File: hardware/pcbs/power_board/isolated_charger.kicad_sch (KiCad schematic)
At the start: 12 parts, among them J4 USB_A, U1 VRB1205S-6WR3, U2 LTV-247, U3 NCP380

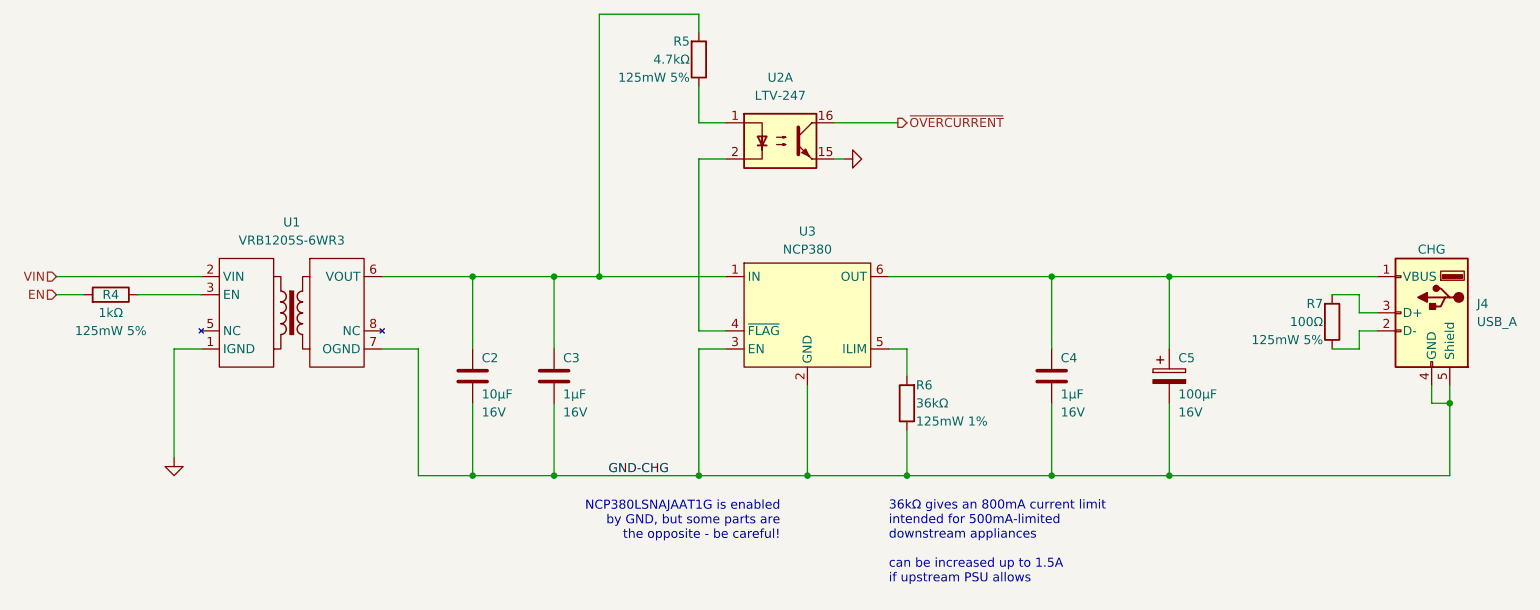
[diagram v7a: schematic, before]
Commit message: power_board: add protection resistor to overload signal
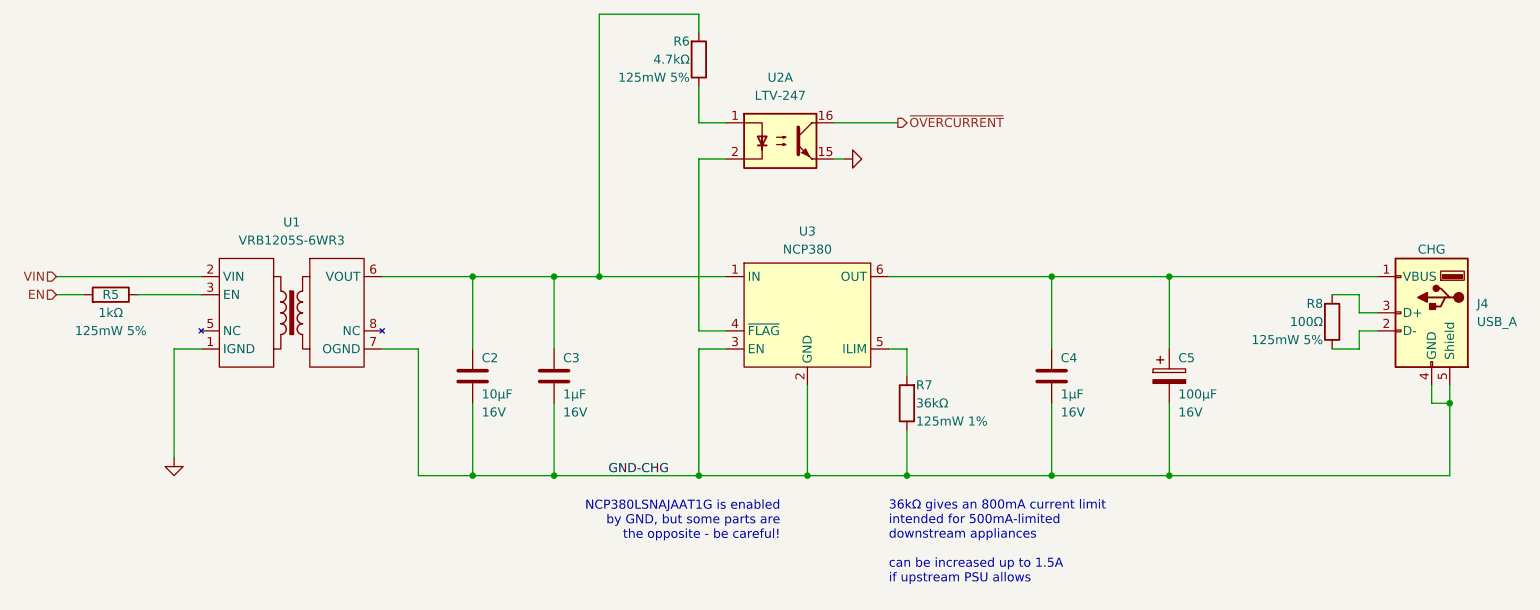
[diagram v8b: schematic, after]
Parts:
- renumbered R4 to R5, R5 to R6, R6 to R7, R7 to R8
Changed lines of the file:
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@@
 		(on_board yes)
 		(dnp no)
-		(property "Reference" "R4"
+		(property "Reference" "R5"
 			(at 69.85 91.44 90)
 			(effects
@@
 			(project "power_board"
 				(path "/4b166175-80a4-48c6-994d-6e62a6160b87/2e2b9578-5dbd-4b2d-88fb-256ac9c8dd75/32f9baea-32bc-4a84-b83a-18c67cc6248e"
-					(reference "R4")
+					(reference "R5")
 					(unit 1)
 				)
 				(path "/4b166175-80a4-48c6-994d-6e62a6160b87/2e2b9578-5dbd-4b2d-88fb-256ac9c8dd75/5f362cd5-d351-4250-994a-9f336837035c"
-					(reference "R8")
+					(reference "R9")
 					(unit 1)
 				)
 				(path "/4b166175-80a4-48c6-994d-6e62a6160b87/2e2b9578-5dbd-4b2d-88fb-256ac9c8dd75/6373063e-1125-40d9-b0ec-3e2cb2886aea"
-					(reference "R12")
+					(reference "R13")
 					(unit 1)
 				)
 				(path "/4b166175-80a4-48c6-994d-6e62a6160b87/2e2b9578-5dbd-4b2d-88fb-256ac9c8dd75/bdb69c9c-123a-4faa-b5c1-7130aac5ebc2"
-					(reference "R16")
+					(reference "R17")
 					(unit 1)
 				)
@@
 		(on_board yes)
 		(dnp no)
-		(property "Reference" "R5"
+		(property "Reference" "R6"
 			(at 151.13 55.88 0)
 			(effects
@@
 			(project "power_board"
 				(path "/4b166175-80a4-48c6-994d-6e62a6160b87/2e2b9578-5dbd-4b2d-88fb-256ac9c8dd75/32f9baea-32bc-4a84-b83a-18c67cc6248e"
-					(reference "R5")
+					(reference "R6")
 					(unit 1)
 				)
 				(path "/4b166175-80a4-48c6-994d-6e62a6160b87/2e2b9578-5dbd-4b2d-88fb-256ac9c8dd75/5f362cd5-d351-4250-994a-9f336837035c"
-					(reference "R9")
+					(reference "R10")
 					(unit 1)
 				)
 				(path "/4b166175-80a4-48c6-994d-6e62a6160b87/2e2b9578-5dbd-4b2d-88fb-256ac9c8dd75/6373063e-1125-40d9-b0ec-3e2cb2886aea"
-					(reference "R13")
+					(reference "R14")
 					(unit 1)
 				)
 				(path "/4b166175-80a4-48c6-994d-6e62a6160b87/2e2b9578-5dbd-4b2d-88fb-256ac9c8dd75/bdb69c9c-123a-4faa-b5c1-7130aac5ebc2"
-					(reference "R17")
+					(reference "R18")
 					(unit 1)
 				)
@@
 		(on_board yes)
 		(dnp no)
-		(property "Reference" "R6"
+		(property "Reference" "R7"
 			(at 182.88 104.14 0)
 			(effects
@@
 			(project "power_board"
 				(path "/4b166175-80a4-48c6-994d-6e62a6160b87/2e2b9578-5dbd-4b2d-88fb-256ac9c8dd75/32f9baea-32bc-4a84-b83a-18c67cc6248e"
-					(reference "R6")
+					(reference "R7")
 					(unit 1)
 				)
 				(path "/4b166175-80a4-48c6-994d-6e62a6160b87/2e2b9578-5dbd-4b2d-88fb-256ac9c8dd75/5f362cd5-d351-4250-994a-9f336837035c"
-					(reference "R10")
+					(reference "R11")
 					(unit 1)
 				)
 				(path "/4b166175-80a4-48c6-994d-6e62a6160b87/2e2b9578-5dbd-4b2d-88fb-256ac9c8dd75/6373063e-1125-40d9-b0ec-3e2cb2886aea"
-					(reference "R14")
+					(reference "R15")
 					(unit 1)
 				)
 				(path "/4b166175-80a4-48c6-994d-6e62a6160b87/2e2b9578-5dbd-4b2d-88fb-256ac9c8dd75/bdb69c9c-123a-4faa-b5c1-7130aac5ebc2"
-					(reference "R18")
+					(reference "R19")
 					(unit 1)
 				)
@@
 		(on_board yes)
 		(dnp no)
-		(property "Reference" "R7"
+		(property "Reference" "R8"
 			(at 240.03 92.71 0)
 			(effects
@@
 			(project "power_board"
 				(path "/4b166175-80a4-48c6-994d-6e62a6160b87/2e2b9578-5dbd-4b2d-88fb-256ac9c8dd75/32f9baea-32bc-4a84-b83a-18c67cc6248e"
-					(reference "R7")
+					(reference "R8")
 					(unit 1)
 				)
 				(path "/4b166175-80a4-48c6-994d-6e62a6160b87/2e2b9578-5dbd-4b2d-88fb-256ac9c8dd75/5f362cd5-d351-4250-994a-9f336837035c"
-					(reference "R11")
+					(reference "R12")
 					(unit 1)
 				)
 				(path "/4b166175-80a4-48c6-994d-6e62a6160b87/2e2b9578-5dbd-4b2d-88fb-256ac9c8dd75/6373063e-1125-40d9-b0ec-3e2cb2886aea"
-					(reference "R15")
+					(reference "R16")
 					(unit 1)
 				)
 				(path "/4b166175-80a4-48c6-994d-6e62a6160b87/2e2b9578-5dbd-4b2d-88fb-256ac9c8dd75/bdb69c9c-123a-4faa-b5c1-7130aac5ebc2"
-					(reference "R19")
-					(unit 1)
-				)
+					(reference "R20")
+					(unit 1)
+				)
